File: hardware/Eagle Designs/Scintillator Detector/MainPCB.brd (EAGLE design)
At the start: 90.2 x 95.5 mm, 32 parts, among them J1 503763-0591, J2 503763-0591, U1 LT1807IS8PBF, U2 LT3461AES6TRMPBF, U3 TMP36FSZ

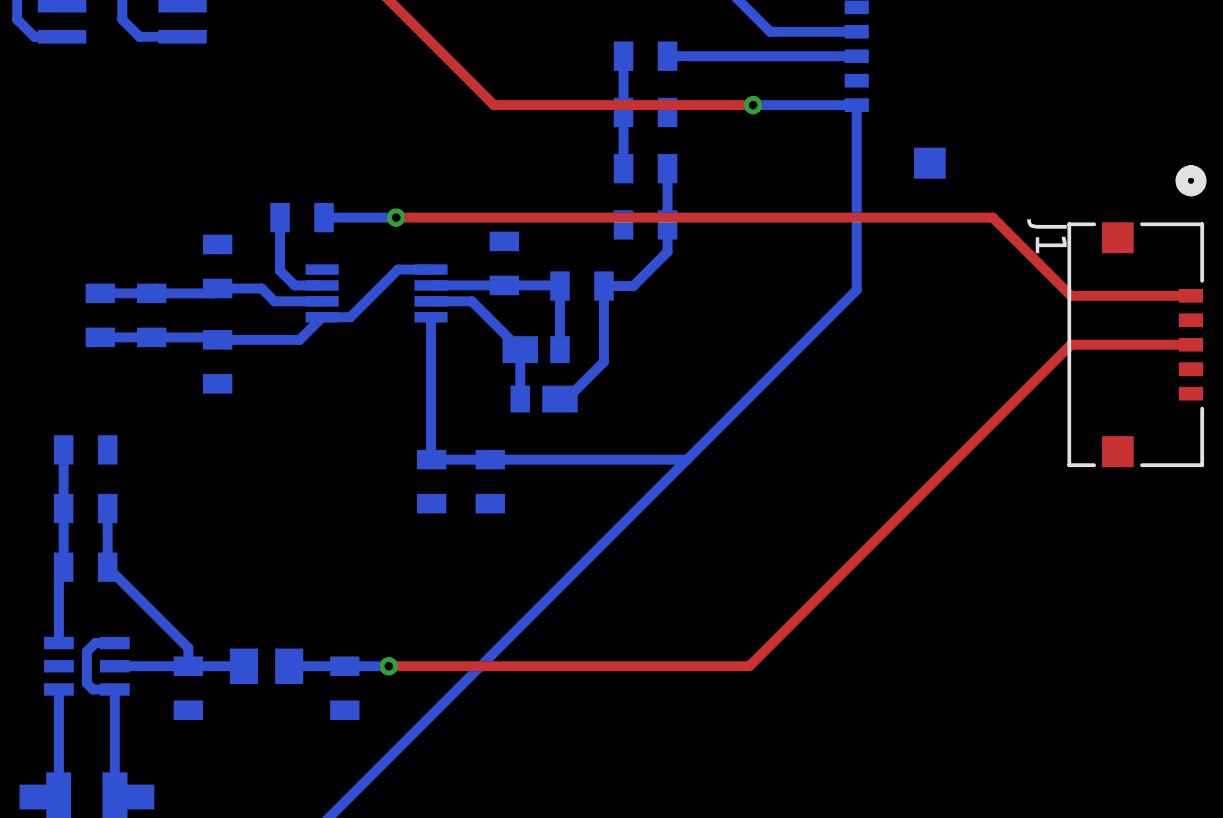
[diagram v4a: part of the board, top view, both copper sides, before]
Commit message: Edited detector pcb and created battery charging circuit board
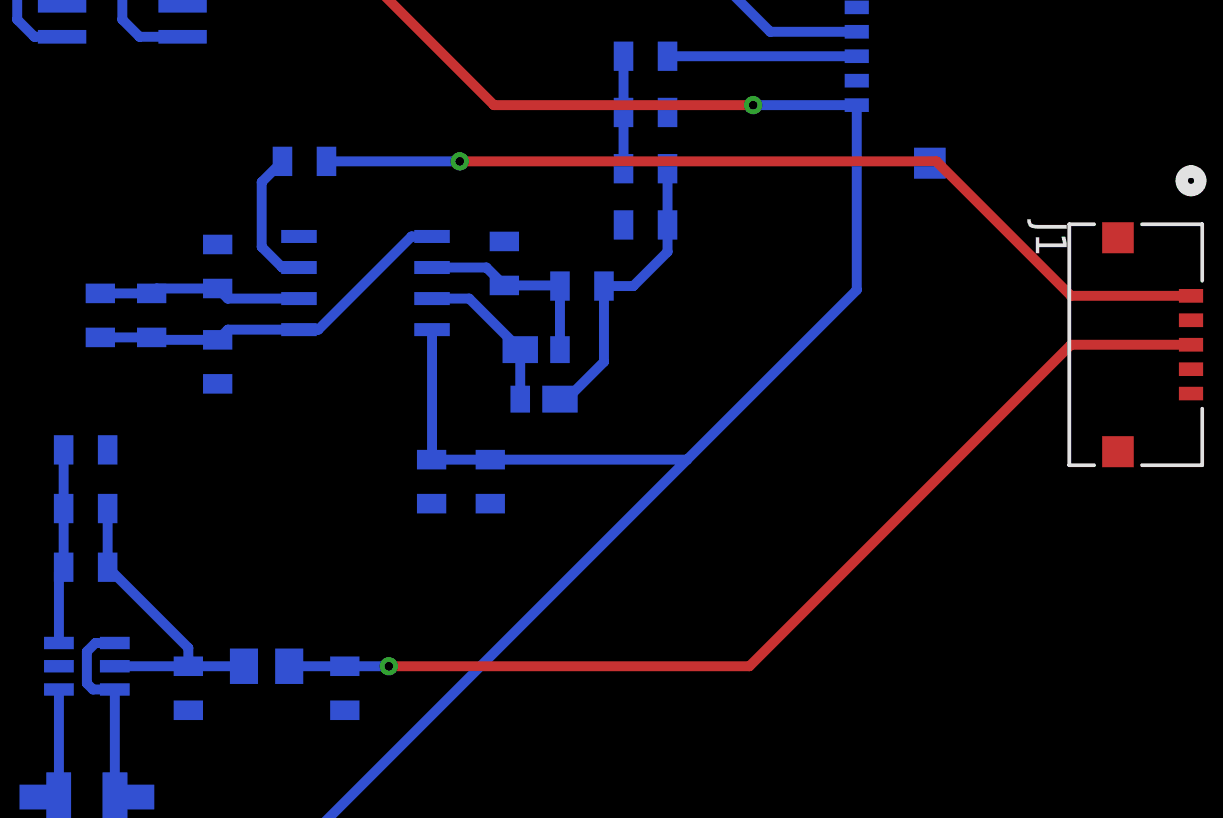
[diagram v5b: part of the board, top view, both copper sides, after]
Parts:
- moved R1 2.30 mm to (40.4, 54.6)
- moved U1 0.64 mm to (42.9, 49.6)
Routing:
- net N$1: track 4.15 -> 5.73 mm
- net N$2: track 9.66 -> 8.38 mm
- net SIPM_SIG: track 36.8 -> 37.6 mm
- net 5V: track 113.8 -> 113.3 mm
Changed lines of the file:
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@@
 </autorouter>
 <elements>
-<element name="U1" library="LT1807" package="MSOP-8_MS_LIT" value="LT1807IS8PBF" x="43.3" y="49.2" smashed="yes" rot="MR180">
-<attribute name="COPYRIGHT" value="Copyright (C) 2021 Ultra Librarian. All rights reserved." x="43.3" y="49.2" size="1.778" layer="28" rot="MR180" display="off"/>
-<attribute name="DIGI-KEY_PART_NUMBER_1" value="LT1807IS8#PBF-ND" x="43.3" y="49.2" size="1.778" layer="28" rot="MR180" display="off"/>
-<attribute name="MANUFACTURER_PART_NUMBER" value="LT1807IS8#PBF" x="43.3" y="49.2" size="1.778" layer="28" rot="MR180" display="off"/>
-<attribute name="MFR_NAME" value="Analog Devices / Linear Technology" x="43.3" y="49.2" size="1.778" layer="28" rot="MR180" display="off"/>
-<attribute name="NAME" x="44.9766" y="46.565" size="0.8128" layer="26" ratio="6" rot="SMR0"/>
+<element name="U1" library="LT1807" package="MSOP-8_MS_LIT" value="LT1807IS8PBF" x="42.85" y="49.65" smashed="yes" rot="MR180">
+<attribute name="COPYRIGHT" value="Copyright (C) 2021 Ultra Librarian. All rights reserved." x="42.85" y="49.65" size="1.778" layer="28" rot="MR180" display="off"/>
+<attribute name="DIGI-KEY_PART_NUMBER_1" value="LT1807IS8#PBF-ND" x="42.85" y="49.65" size="1.778" layer="28" rot="MR180" display="off"/>
+<attribute name="MANUFACTURER_PART_NUMBER" value="LT1807IS8#PBF" x="42.85" y="49.65" size="1.778" layer="28" rot="MR180" display="off"/>
+<attribute name="MFR_NAME" value="Analog Devices / Linear Technology" x="42.85" y="49.65" size="1.778" layer="28" rot="MR180" display="off"/>
+<attribute name="NAME" x="44.9266" y="46.015" size="0.8128" layer="26" ratio="6" rot="SMR0"/>
 </element>
 <element name="U2" library="LT3461" package="TSOT-23_S6" value="LT3461AES6TRMPBF" x="31.45" y="33.95" smashed="yes" rot="MR180">
@@
 <attribute name="PURCHASE-URL" value="https://pricing.snapeda.com/search/part/LT3461AES6#TRMPBF/?ref=eda" x="31.45" y="33.95" size="1.778" layer="28" rot="MR180" display="off"/>
 </element>
-<element name="R1" library="HSFL_Main_Library" package="0805" value="1k" x="40.25" y="52.3" smashed="yes" rot="MR0">
-<attribute name="NAME" x="42.028" y="53.3795" size="0.8128" layer="26" font="vector" ratio="15" rot="SMR0"/>
+<element name="R1" library="HSFL_Main_Library" package="0805" value="1k" x="40.35" y="54.6" smashed="yes" rot="MR0">
+<attribute name="NAME" x="42.128" y="55.6795" size="0.8128" layer="26" font="vector" ratio="15" rot="SMR0"/>
 </element>
 <element name="R2" library="HSFL_Main_Library" package="0805" value="249" x="36.8" y="50.3" smashed="yes" rot="MR270">
@@
 <contactref element="U1" pad="3"/>
 <contactref element="R1" pad="2"/>
-<wire x1="39.35" y1="52.3" x2="39.35" y2="50.125" width="0.4064" layer="16"/>
-<wire x1="39.35" y1="50.125" x2="39.95" y2="49.525" width="0.4064" layer="16"/>
-<wire x1="39.95" y1="49.525" x2="41.073953125" y2="49.525" width="0.4064" layer="16"/>
+<wire x1="39.45" y1="54.6" x2="38.6" y2="53.75" width="0.4064" layer="16"/>
+<wire x1="38.6" y1="53.75" x2="38.6" y2="51.1" width="0.4064" layer="16"/>
+<wire x1="38.6" y1="51.1" x2="39.442" y2="50.258" width="0.4064" layer="16"/>
+<wire x1="39.442" y1="50.258" x2="40.124653125" y2="50.258" width="0.4064" layer="16"/>
 </signal>
 <signal name="SIPM_SIG">
 <contactref element="R1" pad="1"/>
 <contactref element="J1" pad="1"/>
-<wire x1="41.15" y1="52.3" x2="44.1" y2="52.3" width="0.4064" layer="16"/>
-<via x="44.1" y="52.3" extent="1-16" drill="0.35"/>
-<wire x1="44.1" y1="52.3" x2="68.5" y2="52.3" width="0.4064" layer="1"/>
-<wire x1="68.5" y1="52.3" x2="71.7" y2="49.1" width="0.4064" layer="1"/>
 <wire x1="71.7" y1="49.1" x2="76.6108" y2="49.1" width="0.4064" layer="1"/>
+<wire x1="41.25" y1="54.6" x2="46.7" y2="54.6" width="0.4064" layer="16"/>
+<via x="46.7" y="54.6" extent="1-16" drill="0.35"/>
+<wire x1="46.7" y1="54.6" x2="66.2" y2="54.6" width="0.4064" layer="1"/>
+<wire x1="66.2" y1="54.6" x2="71.7" y2="49.1" width="0.4064" layer="1"/>
 </signal>
 <signal name="N$2">
@@
 <contactref element="R3" pad="1"/>
 <contactref element="C3" pad="1"/>
-<wire x1="41.073953125" y1="48.875" x2="39.125" y2="48.875" width="0.4064" layer="16"/>
-<wire x1="39.125" y1="48.875" x2="38.6" y2="49.4" width="0.4064" layer="16"/>
-<wire x1="38.6" y1="49.4" x2="36.8" y2="49.4" width="0.4064" layer="16"/>
 <wire x1="34.3" y1="49.4" x2="34.1" y2="49.2" width="0.4064" layer="16"/>
 <wire x1="32" y1="49.2" x2="34.1" y2="49.2" width="0.4064" layer="16"/>
-<wire x1="34.1" y1="49.2" x2="36.6" y2="49.2" width="0.4064" layer="16"/>
-<wire x1="36.6" y1="49.2" x2="36.8" y2="49.4" width="0.4064" layer="16"/>
+<wire x1="40.124653125" y1="48.988" x2="37.212" y2="48.988" width="0.4064" layer="16"/>
+<wire x1="37.212" y1="48.988" x2="36.8" y2="49.4" width="0.4064" layer="16"/>
+<wire x1="36.8" y1="49.4" x2="34.3" y2="49.4" width="0.4064" layer="16"/>
 </signal>
 <signal name="N$4">
@@
 <contactref element="D2" pad="+"/>
 <wire x1="50.8" y1="49.5" x2="50.8" y2="46.9" width="0.4064" layer="16"/>
-<wire x1="45.526046875" y1="49.525" x2="48.525" y2="49.525" width="0.4064" layer="16"/>
 <wire x1="48.525" y1="49.525" x2="50.775" y2="49.525" width="0.4064" layer="16"/>
 <wire x1="50.775" y1="49.525" x2="50.8" y2="49.5" width="0.4064" layer="16"/>
+<wire x1="45.567346875" y1="50.258" x2="47.792" y2="50.258" width="0.4064" layer="16"/>
+<wire x1="47.792" y1="50.258" x2="48.525" y2="49.525" width="0.4064" layer="16"/>
 </signal>
 <signal name="N$6">
@@
 <contactref element="D2" pad="-"/>
 <wire x1="49.175" y1="44.875" x2="49.175" y2="46.9" width="0.4064" layer="16"/>
-<wire x1="45.526046875" y1="48.875" x2="47.2" y2="48.875" width="0.4064" layer="16"/>
-<wire x1="47.2" y1="48.875" x2="49.175" y2="46.9" width="0.4064" layer="16"/>
+<wire x1="45.567346875" y1="48.988" x2="47.087" y2="48.988" width="0.4064" layer="16"/>
+<wire x1="47.087" y1="48.988" x2="49.175" y2="46.9" width="0.4064" layer="16"/>
 </signal>
 <signal name="N$5">
@@
 <wire x1="31.45" y1="33.25" x2="31.7" y2="33" width="0.4064" layer="16"/>
 <wire x1="31.7" y1="33" x2="32.593" y2="33" width="0.4064" layer="16"/>
-<wire x1="45.526046875" y1="48.225" x2="45.526046875" y2="42.423953125" width="0.4064" layer="16"/>
-<wire x1="45.526046875" y1="42.423953125" x2="45.55" y2="42.4" width="0.4064" layer="16"/>
 <wire x1="45.55" y1="42.4" x2="47.95" y2="42.4" width="0.4064" layer="16"/>
 <wire x1="47.95" y1="42.4" x2="56" y2="42.4" width="0.4064" layer="16"/>
@@
 <via x="41.5" y="63.5" extent="1-16" drill="0.35"/>
 <wire x1="41.5" y1="63.5" x2="38.1" y2="63.5" width="0.4064" layer="16"/>
+<wire x1="45.567346875" y1="47.718" x2="45.567346875" y2="42.417346875" width="0.4064" layer="16"/>
+<wire x1="45.567346875" y1="42.417346875" x2="45.55" y2="42.4" width="0.4064" layer="16"/>
 </signal>
 <signal name="N$7">
@@
 <contactref element="U2" pad="5"/>
 <contactref element="C7" pad="1"/>
-<wire x1="35.4" y1="33.95" x2="35.6" y2="33.95" width="0.4064" layer="16"/>
 <contactref element="L2" pad="2"/>
 <wire x1="32.3" y1="40.4" x2="32.3" y2="38" width="0.4064" layer="16"/>
+<wire x1="35.6" y1="33.95" x2="35.6" y2="34.7" width="0.4064" layer="16"/>
+<wire x1="35.6" y1="34.7" x2="32.3" y2="38" width="0.4064" layer="16"/>
 <wire x1="32.593" y1="33.95" x2="35.6" y2="33.95" width="0.4064" layer="16"/>
 <wire x1="35.6" y1="33.95" x2="37.875" y2="33.95" width="0.4064" layer="16"/>
-<wire x1="35.6" y1="33.95" x2="35.6" y2="34.7" width="0.4064" layer="16"/>
-<wire x1="35.6" y1="34.7" x2="32.3" y2="38" width="0.4064" layer="16"/>
 </signal>
 <signal name="SIPM_PWR">
@@
 <contactref element="U1" pad="1"/>
 <contactref element="C3" pad="2"/>
+<wire x1="34.1" y1="47.4" x2="32" y2="47.4" width="0.4064" layer="16"/>
+<wire x1="40.124653125" y1="47.718" x2="37.218" y2="47.718" width="0.4064" layer="16"/>
+<wire x1="37.218" y1="47.718" x2="36.8" y2="47.3" width="0.4064" layer="16"/>
+<wire x1="36.8" y1="47.3" x2="34.2" y2="47.3" width="0.4064" layer="16"/>
 <wire x1="34.2" y1="47.3" x2="34.1" y2="47.4" width="0.4064" layer="16"/>
-<wire x1="36.8" y1="47.3" x2="40.148953125" y2="47.3" width="0.4064" layer="16"/>
-<wire x1="40.148953125" y1="47.3" x2="41.073953125" y2="48.225" width="0.4064" layer="16"/>
-<wire x1="41.073953125" y1="48.225" x2="42.225" y2="48.225" width="0.4064" layer="16"/>
-<wire x1="42.225" y1="48.225" x2="44.175" y2="50.175" width="0.4064" layer="16"/>
-<wire x1="44.175" y1="50.175" x2="45.526046875" y2="50.175" width="0.4064" layer="16"/>
-<wire x1="34.1" y1="47.4" x2="32" y2="47.4" width="0.4064" layer="16"/>
-<wire x1="34.1" y1="47.4" x2="36.7" y2="47.4" width="0.4064" layer="16"/>
-<wire x1="36.7" y1="47.4" x2="36.8" y2="47.3" width="0.4064" layer="16"/>
+<wire x1="40.124653125" y1="47.718" x2="40.918" y2="47.718" width="0.4064" layer="16"/>
+<wire x1="44.728" y1="51.528" x2="45.567346875" y2="51.528" width="0.4064" layer="16"/>
+<wire x1="40.918" y1="47.718" x2="44.728" y2="51.528" width="0.4064" layer="16"/>
 </signal>
 </signals>
